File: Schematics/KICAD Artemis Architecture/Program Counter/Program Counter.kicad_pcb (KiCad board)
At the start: 4 copper layers, 62.6 x 31.6 mm, 26 parts, among them J1 Bus, J2 Power, J3 Control, Q1 2N3904, U1 74LS161, U2 74LS161, U3 74LS245

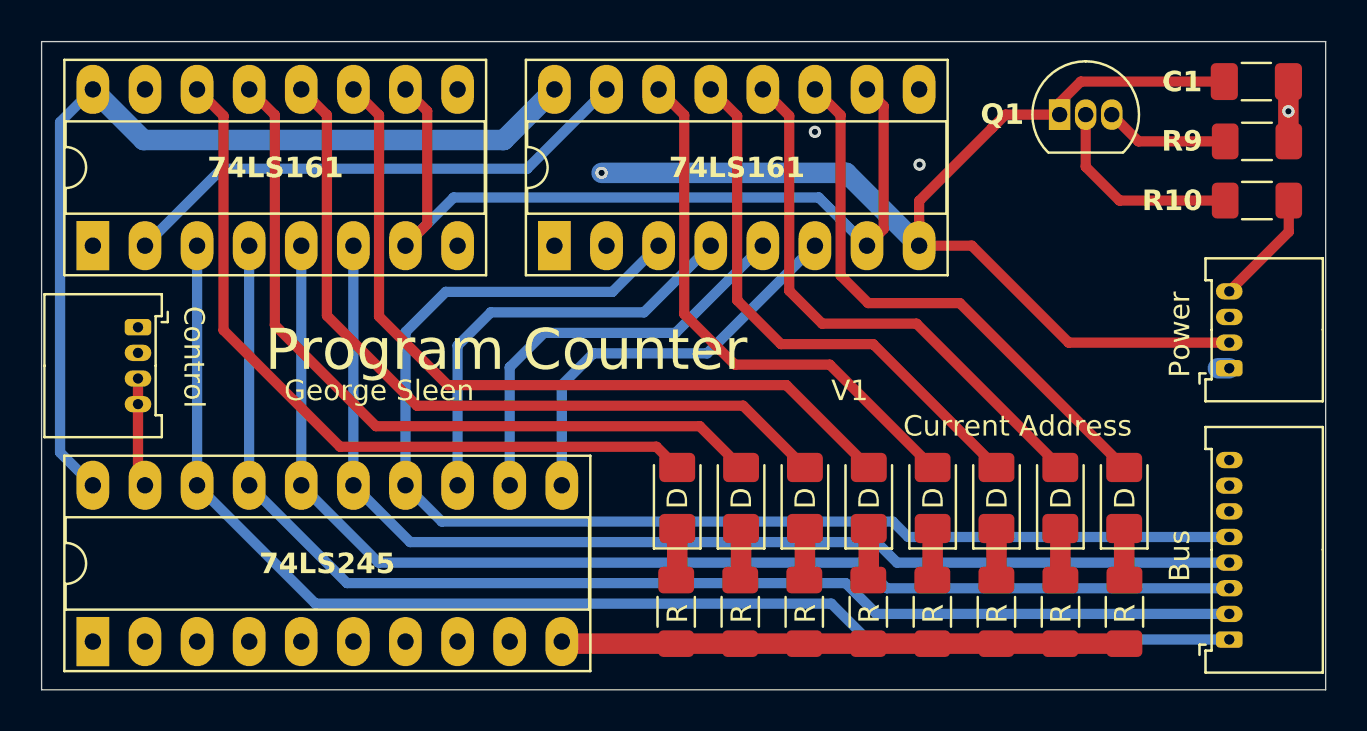
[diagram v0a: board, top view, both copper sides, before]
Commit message: Started Memory PCB
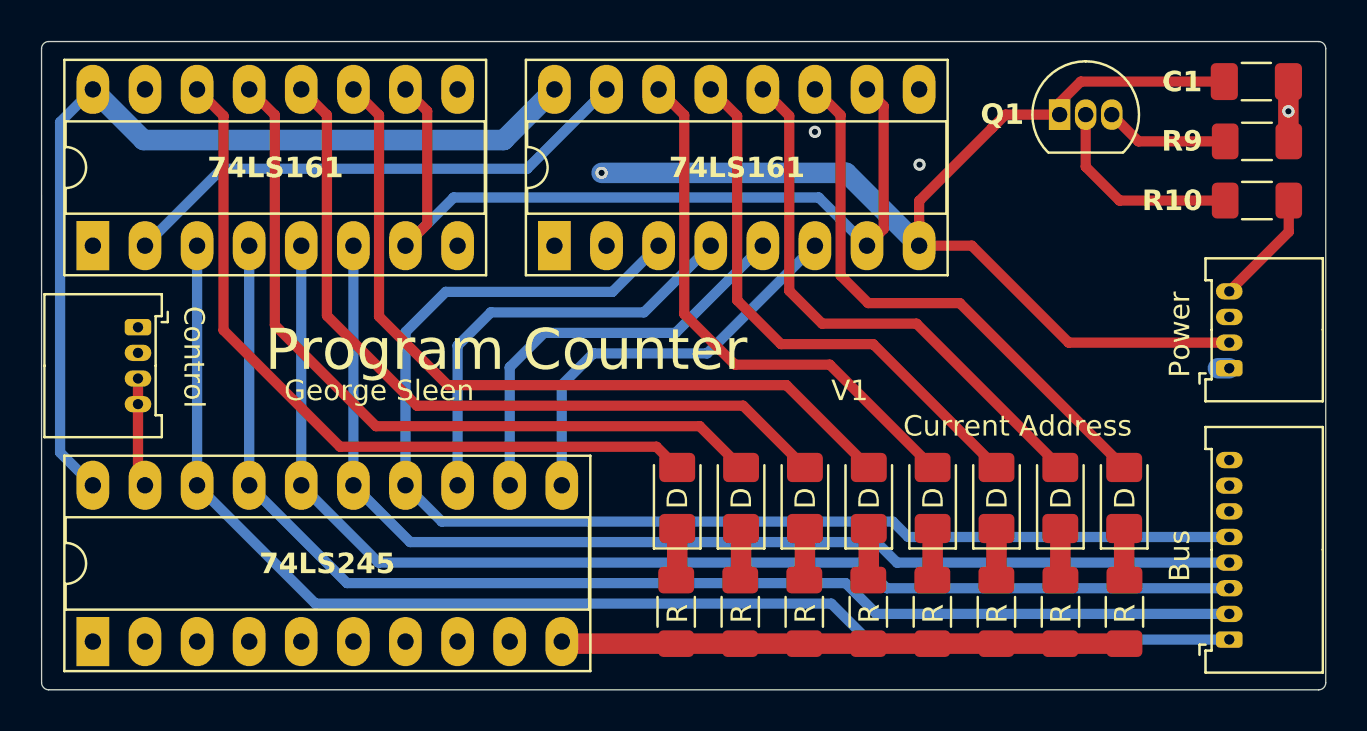
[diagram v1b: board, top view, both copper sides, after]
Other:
- outline, holes or cut-outs redrawn
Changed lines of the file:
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@@
 		)
 		(property "Value" "0.1uF"
-			(at 0 1.85 360)
+			(at 0 1.85 0)
 			(layer "F.Fab")
 			(effects
@@
 		)
 		(fp_text user "${REFERENCE}"
-			(at 0 0 360)
+			(at 0 0 0)
 			(layer "F.Fab")
 			(effects
@@
 		(tags "to-92 sc-43 sc-43a sot54 PA33 transistor")
 		(property "Reference" "Q1"
-			(at 1.27 -3.56 360)
+			(at 1.27 -3.56 0)
 			(layer "F.SilkS")
 			(hide yes)
@@
 		)
 		(property "Value" "2N3904"
-			(at 1.27 2.79 360)
+			(at 1.27 2.79 0)
 			(layer "F.Fab")
 			(effects
@@
 		)
 		(fp_text user "${REFERENCE}"
-			(at 1.27 0 360)
+			(at 1.27 0 0)
 			(layer "F.Fab")
 			(effects
@@
 		)
 	)
-	(gr_rect
-		(start 101.7 61)
-		(end 164.3 92.6)
+	(gr_line
+		(start 102.047487 60.997487)
+		(end 163.952513 60.997487)
+		(stroke
+			(width 0.05)
+			(type default)
+		)
+		(layer "Edge.Cuts")
+	)
+	(gr_line
+		(start 163.952513 92.602513)
+		(end 102.05 92.6)
+		(stroke
+			(width 0.05)
+			(type default)
+		)
+		(layer "Edge.Cuts")
+	)
+	(gr_arc
+		(start 163.952513 60.997487)
+		(mid 164.2 61.1)
+		(end 164.302513 61.347487)
+		(stroke
+			(width 0.05)
+			(type default)
+		)
+		(layer "Edge.Cuts")
+	)
+	(gr_arc
+		(start 102.05 92.6)
+		(mid 101.802513 92.497487)
+		(end 101.7 92.25)
+		(stroke
+			(width 0.05)
+			(type default)
+		)
+		(layer "Edge.Cuts")
+	)
+	(gr_arc
+		(start 101.697487 61.347487)
+		(mid 101.8 61.1)
+		(end 102.047487 60.997487)
+		(stroke
+			(width 0.05)
+			(type default)
+		)
+		(layer "Edge.Cuts")
+	)
+	(gr_line
+		(start 164.302513 61.347487)
+		(end 164.302513 92.252513)
+		(stroke
+			(width 0.05)
+			(type default)
+		)
+		(layer "Edge.Cuts")
+	)
+	(gr_arc
+		(start 164.302513 92.252513)
+		(mid 164.2 92.5)
+		(end 163.952513 92.602513)
+		(stroke
+			(width 0.05)
+			(type default)
+		)
+		(layer "Edge.Cuts")
+	)
+	(gr_line
+		(start 101.7 92.25)
+		(end 101.697487 61.347487)
 		(stroke
 			(width 0.05)
 			(type default)
 		)
-		(fill none)
 		(layer "Edge.Cuts")
 	)

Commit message: Rounded Corners on PC PCB
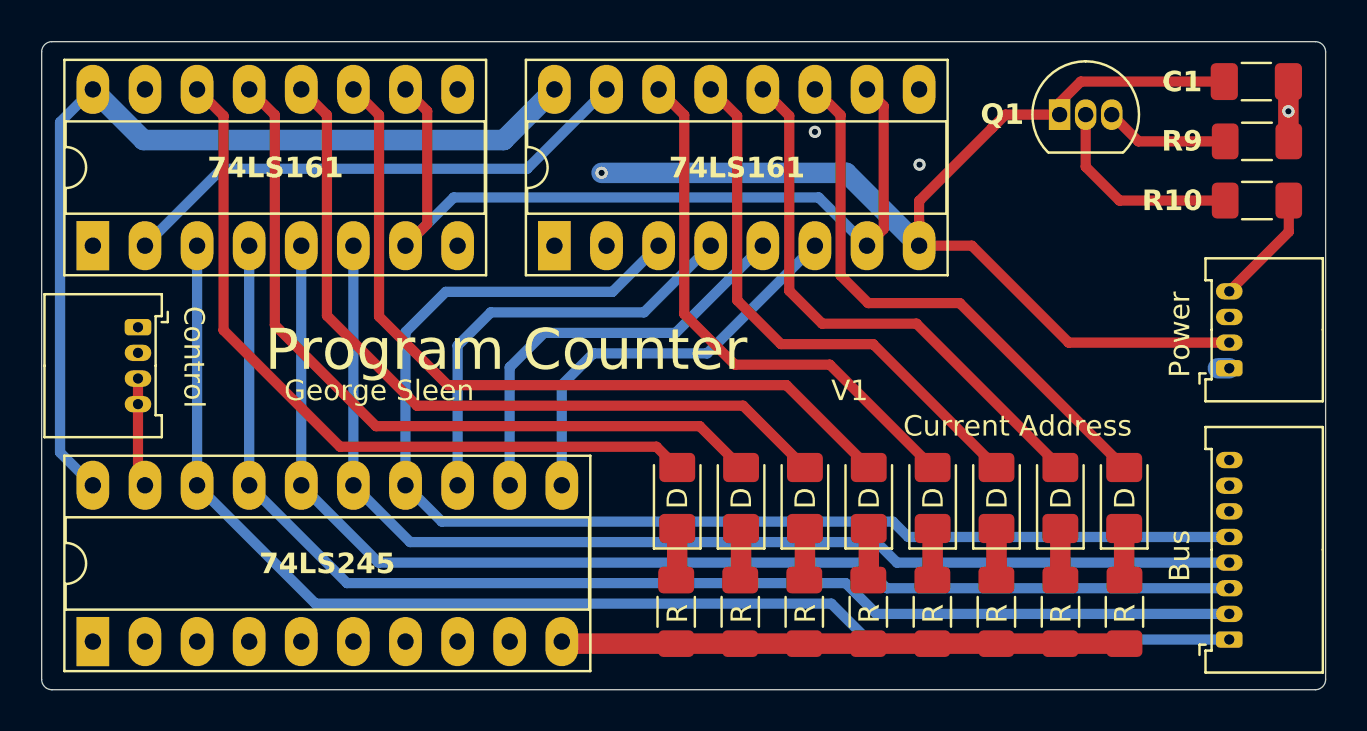
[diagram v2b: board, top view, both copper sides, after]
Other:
- outline, holes or cut-outs redrawn
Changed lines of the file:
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@@
 	)
 	(gr_line
-		(start 102.047487 60.997487)
-		(end 163.952513 60.997487)
+		(start 102.203553 61.003553)
+		(end 163.796447 61.003553)
+		(stroke
+			(width 0.05)
+			(type default)
+		)
+		(layer "Edge.Cuts")
+	)
+	(gr_arc
+		(start 101.703553 61.503553)
+		(mid 101.85 61.15)
+		(end 102.203553 61.003553)
+		(stroke
+			(width 0.05)
+			(type default)
+		)
+		(layer "Edge.Cuts")
+	)
+	(gr_arc
+		(start 163.796447 61.003553)
+		(mid 164.15 61.15)
+		(end 164.296447 61.503553)
+		(stroke
+			(width 0.05)
+			(type default)
+		)
+		(layer "Edge.Cuts")
+	)
+	(gr_arc
+		(start 102.203553 92.596447)
+		(mid 101.85 92.45)
+		(end 101.703553 92.096447)
 		(stroke
 			(width 0.05)
@@
 	)
 	(gr_line
-		(start 163.952513 92.602513)
-		(end 102.05 92.6)
+		(start 163.796447 92.596447)
+		(end 102.203553 92.596447)
+		(stroke
+			(width 0.05)
+			(type default)
+		)
+		(layer "Edge.Cuts")
+	)
+	(gr_line
+		(start 164.296447 61.503553)
+		(end 164.296447 92.096447)
+		(stroke
+			(width 0.05)
+			(type default)
+		)
+		(layer "Edge.Cuts")
+	)
+	(gr_line
+		(start 101.703553 92.096447)
+		(end 101.703553 61.503553)
 		(stroke
 			(width 0.05)
@@
 	)
 	(gr_arc
-		(start 163.952513 60.997487)
-		(mid 164.2 61.1)
-		(end 164.302513 61.347487)
+		(start 164.296447 92.096447)
+		(mid 164.15 92.45)
+		(end 163.796447 92.596447)
 		(stroke
 			(width 0.05)
-			(type default)
-		)
-		(layer "Edge.Cuts")
-	)
-	(gr_arc
-		(start 102.05 92.6)
-		(mid 101.802513 92.497487)
-		(end 101.7 92.25)
-		(stroke
-			(width 0.05)
-			(type default)
-		)
-		(layer "Edge.Cuts")
-	)
-	(gr_arc
-		(start 101.697487 61.347487)
-		(mid 101.8 61.1)
-		(end 102.047487 60.997487)
-		(stroke
-			(width 0.05)
-			(type default)
-		)
-		(layer "Edge.Cuts")
-	)
-	(gr_line
-		(start 164.302513 61.347487)
-		(end 164.302513 92.252513)
-		(stroke
-			(width 0.05)
-			(type default)
-		)
-		(layer "Edge.Cuts")
-	)
-	(gr_arc
-		(start 164.302513 92.252513)
-		(mid 164.2 92.5)
-		(end 163.952513 92.602513)
-		(stroke
-			(width 0.05)
-			(type default)
-		)
-		(layer "Edge.Cuts")
-	)
-	(gr_line
-		(start 101.7 92.25)
-		(end 101.697487 61.347487)
-		(stroke
-			(width 0.05)

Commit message: Program Memory
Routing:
- net VCC: track 154.8 -> 153.3 mm
- net GNDREF: track 82.6 -> 81.3 mm
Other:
- outline, holes or cut-outs redrawn
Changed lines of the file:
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@@
 		)
 	)
-	(gr_line
-		(start 102.203553 61.003553)
-		(end 163.796447 61.003553)
+	(gr_arc
+		(start 101.7 62)
+		(mid 101.992893 61.292893)
+		(end 102.7 61)
 		(stroke
 			(width 0.05)
@@
 		(layer "Edge.Cuts")
 	)
-	(gr_arc
-		(start 101.703553 61.503553)
-		(mid 101.85 61.15)
-		(end 102.203553 61.003553)
+	(gr_line
+		(start 164.3 62)
+		(end 164.3 91.6)
 		(stroke
 			(width 0.05)
@@
 	)
 	(gr_arc
-		(start 163.796447 61.003553)
-		(mid 164.15 61.15)
-		(end 164.296447 61.503553)
+		(start 164.3 91.6)
+		(mid 164.007107 92.307107)
+		(end 163.3 92.6)
 		(stroke
 			(width 0.05)
@@
 		(layer "Edge.Cuts")
 	)
-	(gr_arc
-		(start 102.203553 92.596447)
-		(mid 101.85 92.45)
-		(end 101.703553 92.096447)
+	(gr_line
+		(start 101.7 91.6)
+		(end 101.7 62)
 		(stroke
 			(width 0.05)
@@
 	)
 	(gr_line
-		(start 163.796447 92.596447)
-		(end 102.203553 92.596447)
+		(start 163.3 92.6)
+		(end 102.7 92.6)
 		(stroke
 			(width 0.05)
@@
 		(layer "Edge.Cuts")
 	)
-	(gr_line
-		(start 164.296447 61.503553)
-		(end 164.296447 92.096447)
+	(gr_arc
+		(start 102.7 92.6)
+		(mid 101.992893 92.307107)
+		(end 101.7 91.6)
 		(stroke
 			(width 0.05)
@@
 	)
 	(gr_line
-		(start 101.703553 92.096447)
-		(end 101.703553 61.503553)
+		(start 102.7 61)
+		(end 163.3 61)
 		(stroke
 			(width 0.05)
@@
 	)
 	(gr_arc
-		(start 164.296447 92.096447)
-		(mid 164.15 92.45)
-		(end 163.796447 92.596447)
+		(start 163.3 61)
+		(mid 164.007107 61.292893)
+		(end 164.3 62)
 		(stroke
 			(width 0.05)
@@
 	)
 	(segment
-		(start 144.48 70.95)
-		(end 144.48 69.72)
-		(width 0.5)
-		(layer "F.Cu")
-		(net 2)
-	)
-	(segment
 		(start 135.758984 90.35)
 		(end 138.88082 90.35)
@@
 	)
 	(segment
-		(start 148.025 65.225)
-		(end 144.48 68.77)
+		(start 144.48 68.77)
+		(end 148.69 64.56)
 		(width 0.5)
 		(layer "F.Cu")
@@
 		(start 152.36 62.95)
 		(end 159.3575 62.95)
-		(width 0.5)
-		(layer "F.Cu")
-		(net 2)
-	)
-	(segment
-		(start 148.025 65.225)
-		(end 148.69 64.56)
 		(width 0.5)
 		(layer "F.Cu")
@@
 	)
 	(segment
-		(start 104.2 63.33)
-		(end 103.92 63.33)
-		(width 1)
-		(layer "In2.Cu")
-		(net 11)
-	)
-	(segment
 		(start 102.6 64.93)
 		(end 104.2 63.33)
@@
 		(layer "B.Cu")
 		(net 11)
-	)
-	(segment
-		(start 126.7 63.33)
-		(end 126.7 63.95)
-		(width 1)
-		(layer "B.Cu")
-		(net 11)
-	)
-	(segment
-		(start 159.044365 76.925)
-		(end 159.6 76.925)
-		(width 1)
-		(layer "B.Cu")
-		(net 11)

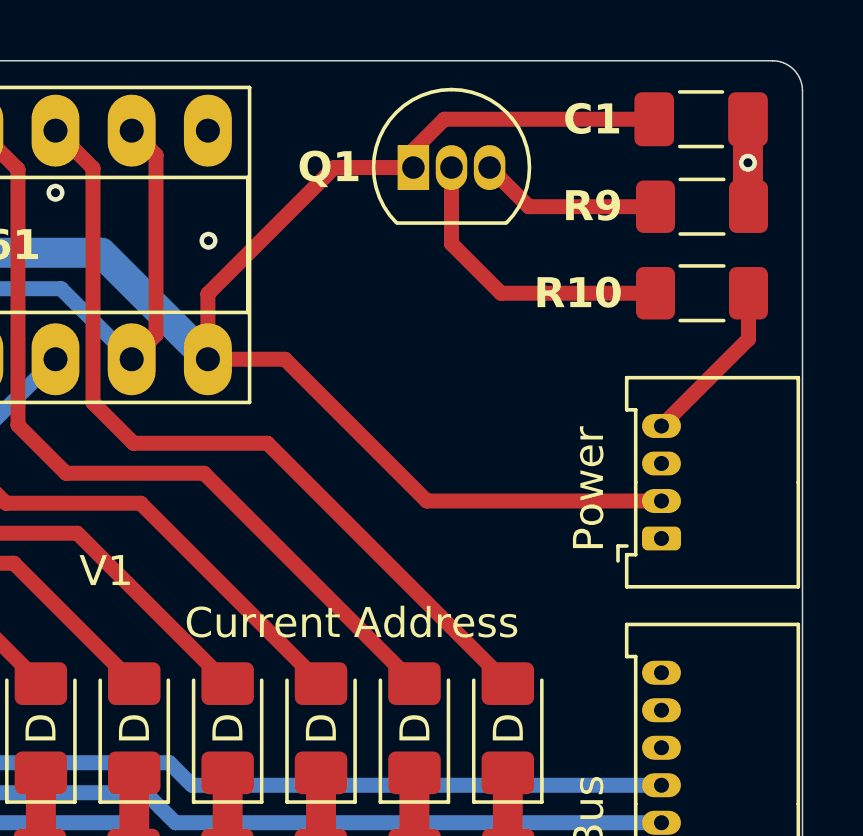
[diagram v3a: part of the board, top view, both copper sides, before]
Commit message: Added Decoupling Caps
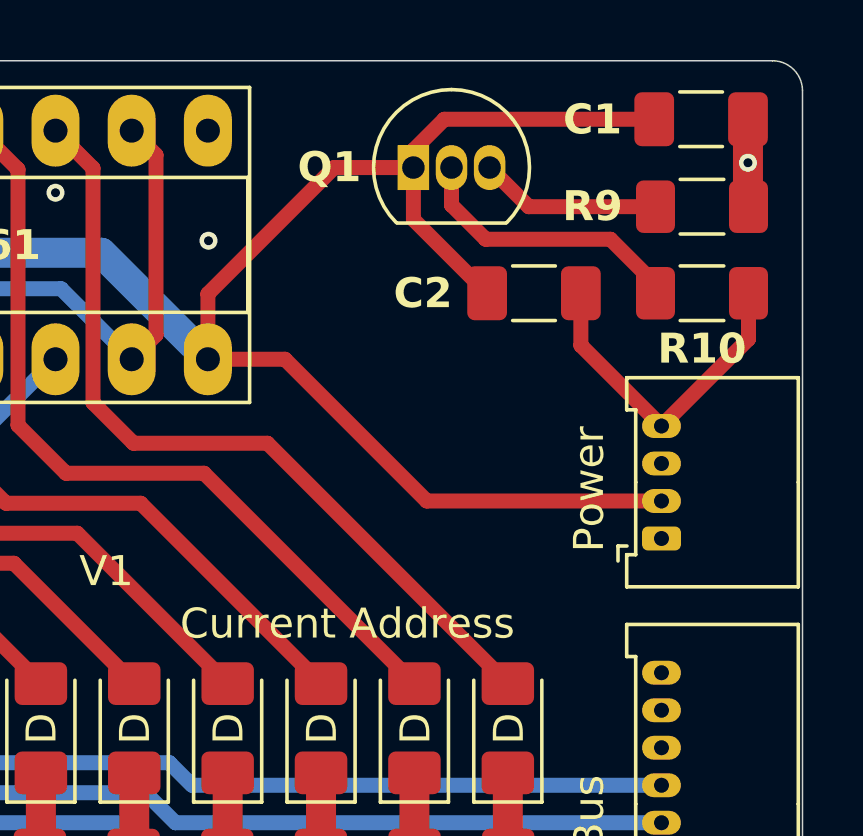
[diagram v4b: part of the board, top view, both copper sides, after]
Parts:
- added C2: 0.1uF, Capacitor_SMD:C_1206_3216Metric_Pad1.33x1.80mm_HandSolder, F.Cu at (155.3, 68.8)
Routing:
- net /CLR: track 5.63 -> 11.2 mm
- net GNDREF: track 81.3 -> 86.5 mm
- net Net-(Q1-B): track 10.0 -> 9.44 mm
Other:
- board text added: "C2"
